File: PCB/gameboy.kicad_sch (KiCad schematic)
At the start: 0 parts

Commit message: [+] pushing to save major progress
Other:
- removed sheet Bank 1
- removed sheet Bank 2
- removed sheet Bank 3
- removed sheet Bank 4
- removed sheet Bank 5
- removed sheet Bank 6
- removed sheet Bank 7
- removed sheet Bank 8
- added sheet DDR (DDR.kicad_sch)
- added sheet FPGA power pins (fpga-power.kicad_sch)

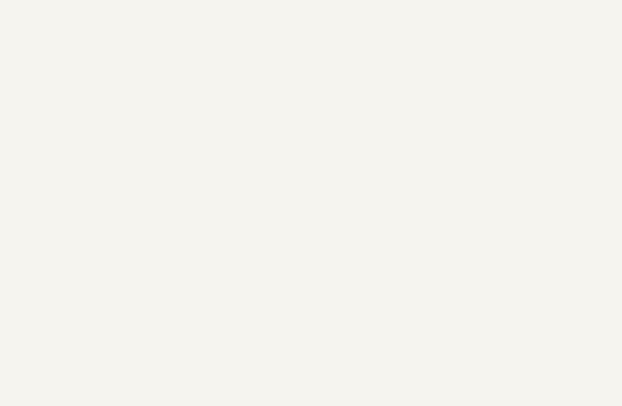
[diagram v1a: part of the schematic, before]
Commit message: added audio_start
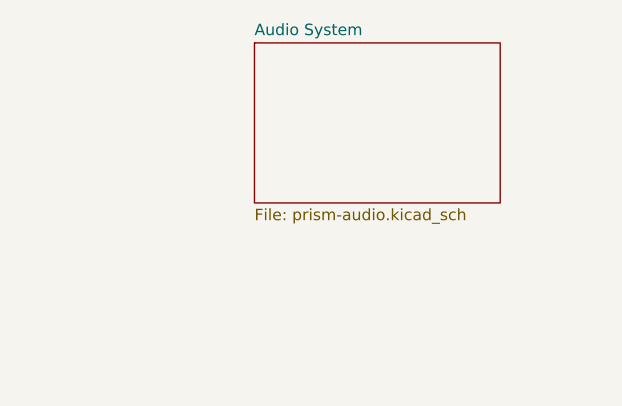
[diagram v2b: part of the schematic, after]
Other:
- added sheet Audio System (prism-audio.kicad_sch)
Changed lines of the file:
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@@
+		)
+	)
+	(sheet
+		(at 161.29 74.93)
+		(size 27.305 17.78)
+		(fields_autoplaced yes)
+		(stroke
+			(width 0.1524)
+			(type solid)
+		)
+		(fill
+			(color 0 0 0 0.0000)
+		)
+		(property "Sheetname" "Audio System"
+			(at 161.29 74.2184 0)
+			(effects
+				(font
+					(size 1.27 1.27)
+				)
+				(justify left bottom)
+			)
+		)
+		(property "Sheetfile" "prism-audio.kicad_sch"
+			(at 161.29 93.2946 0)
+			(effects
+				(font
+					(size 1.27 1.27)
+				)
+				(justify left top)
+			)
+		)
+		(instances
+			(project "gameboy"
+				(path "/bfbf29d7-ad29-43e7-b23f-5805508cd3f0"
+					(page "2")
+				)
+			)
 		)
 	)
